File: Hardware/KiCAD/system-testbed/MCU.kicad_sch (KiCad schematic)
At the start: 1 part, among them U5 ESP32

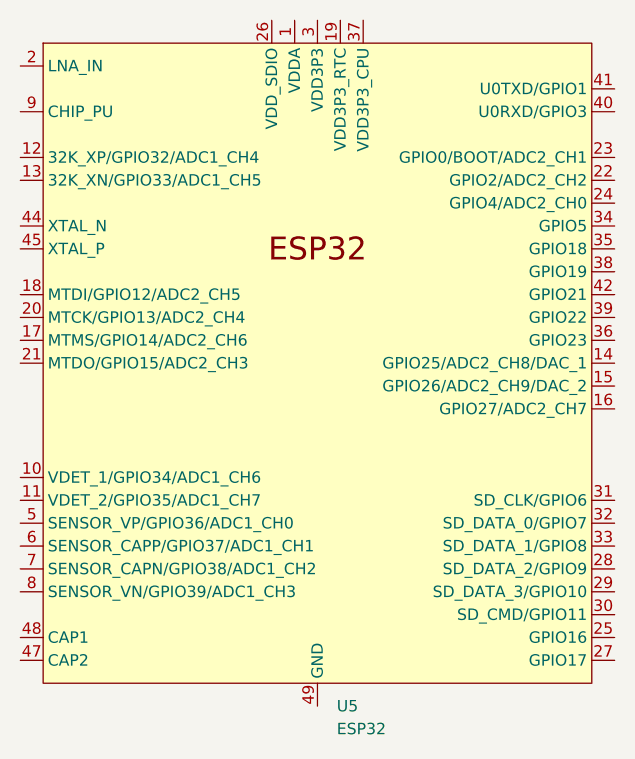
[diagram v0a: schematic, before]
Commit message: fix: added WROVER symbol to project library and schematic
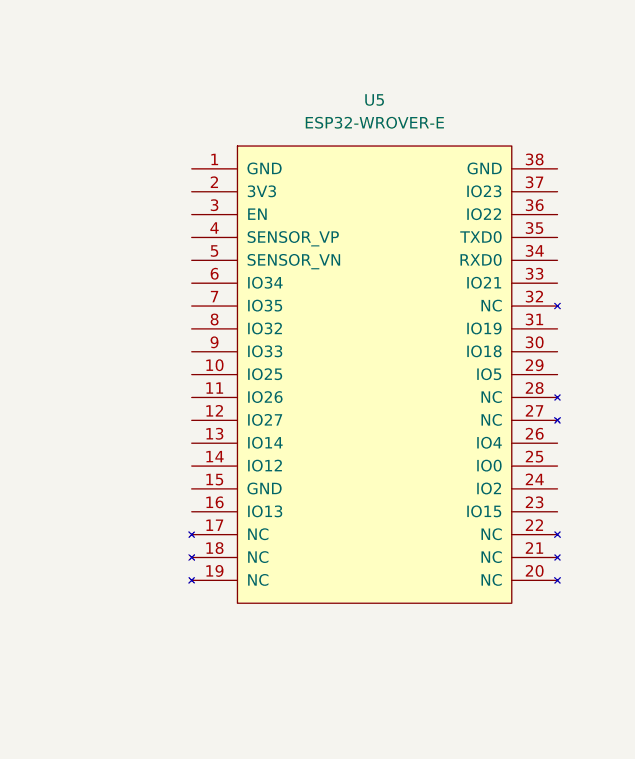
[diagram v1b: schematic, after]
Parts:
- removed U5: ESP32, Package_DFN_QFN:QFN-48-1EP_6x6mm_P0.4mm_EP4.3x4.3mm, symbol capstone-project:ESP32
- added U5: ESP32-WROVER-E, symbol capstone-project:ESP32-WROVER-E
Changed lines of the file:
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@@
 	(paper "A4")
 	(symbol
-		(lib_id "capstone-project:ESP32")
-		(at 140.97 81.28 0)
+		(lib_id "capstone-project:ESP32-WROVER-E")
+		(at 147.32 82.55 0)
 		(unit 1)
 		(exclude_from_sim no)
@@
 		(fields_autoplaced yes)
 		(property "Reference" "U5"
-			(at 143.1133 119.38 0)
+			(at 147.32 52.07 0)
 			(effects
 				(font
 					(size 1.27 1.27)
 				)
-				(justify left)
 			)
 		)
-		(property "Value" "ESP32"
-			(at 143.1133 121.92 0)
+		(property "Value" "ESP32-WROVER-E"
+			(at 147.32 54.61 0)
 			(effects
 				(font
 					(size 1.27 1.27)
 				)
-				(justify left)
 			)
 		)
-		(property "Footprint" "Package_DFN_QFN:QFN-48-1EP_6x6mm_P0.4mm_EP4.3x4.3mm"
-			(at 140.97 129.54 0)
+		(property "Footprint" ""
+			(at 147.32 73.66 0)
 			(effects
 				(font
@@
 			)
 		)
-		(property "Datasheet" "https://www.espressif.com/sites/default/files/documentation/esp32_datasheet_en.pdf"
-			(at 140.97 132.08 0)
+		(property "Datasheet" ""
+			(at 147.32 73.66 0)
 			(effects
 				(font
@@
 			)
 		)
-		(property "Description" "ESP32 is a single 2.4 GHz Wi-Fi-and-Bluetooth combo chip designed with the TSMC ultra-low-power 40 nmtechnology."
-			(at 140.97 81.28 0)
+		(property "Description" ""
+			(at 147.32 82.55 0)
 			(effects
 				(font
@@
 			)
 		)
+		(pin "31"
+		)
+		(pin "6"
+		)
+		(pin "19"
+		)
+		(pin "29"
+		)
+		(pin "3"
+		)
+		(pin "37"
+		)
+		(pin "32"
+		)
+		(pin "38"
+		)
+		(pin "17"
+		)
+		(pin "8"
+		)
+		(pin "34"
+		)
 		(pin "13"
 		)
-		(pin "44"
-		)
-		(pin "45"
+		(pin "14"
 		)
 		(pin "18"
 		)
-		(pin "20"
+		(pin "30"
 		)
-		(pin "17"
-		)
-		(pin "21"
-		)
-		(pin "10"
-		)
-		(pin "11"
-		)
-		(pin "5"
-		)
-		(pin "6"
+		(pin "33"
 		)
 		(pin "7"
 		)
-		(pin "8"
-		)
-		(pin "48"
-		)
-		(pin "47"
-		)
-		(pin "26"
-		)
-		(pin "1"
-		)
-		(pin "43"
-		)
-		(pin "46"
-		)
-		(pin "3"
-		)
-		(pin "4"
-		)
-		(pin "49"
-		)
-		(pin "19"
-		)
-		(pin "37"
-		)
-		(pin "41"
-		)
-		(pin "40"
+		(pin "5"
 		)
 		(pin "23"
@@
 		(pin "22"
 		)
-		(pin "24"
+		(pin "21"
 		)
-		(pin "34"
+		(pin "9"
+		)
+		(pin "16"
+		)
+		(pin "20"
+		)
+		(pin "27"
+		)
+		(pin "26"
+		)
+		(pin "4"
+		)
+		(pin "10"
+		)
+		(pin "36"
+		)
+		(pin "11"
 		)
 		(pin "35"
 		)
-		(pin "38"
+		(pin "28"
 		)
-		(pin "42"
-		)
-		(pin "39"
-		)
-		(pin "36"
-		)
-		(pin "14"
+		(pin "12"
 		)
 		(pin "15"
 		)
-		(pin "16"
-		)
-		(pin "31"
-		)
-		(pin "32"
-		)
-		(pin "33"
-		)
-		(pin "28"
-		)
-		(pin "29"
-		)
-		(pin "30"
-		)
 		(pin "25"
 		)
-		(pin "27"
+		(pin "24"
+		)
+		(pin "1"
 		)
 		(pin "2"
 		)
-		(pin "9"
-		)
-		(pin "12"
-		)
 		(instances
